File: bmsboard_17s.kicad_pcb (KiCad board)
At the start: 2 copper layers, 100 x 90 mm, 181 parts, among them Q1 Q_NMOS_GDS, Q10 Q_NMOS_GDS, Q11 Q_NMOS_GDS, Q12 Q_NMOS_GDS, Q13 Q_NMOS_GDS, Q14 Q_NMOS_GDS, Q15 Q_NMOS_GDS, Q16 Q_NMOS_GDS, Q17 Q_NMOS_GDS, Q18 Q_NMOS_GDS, Q19 Q_NMOS_GDS, Q2 Q_NMOS_GDS, Q20 Q_NMOS_GDS, Q21 Q_NMOS_GDS, Q22 Q_NMOS_GDS, Q23 Q_NMOS_GDS, Q24 Q_NMOS_GDS, Q25 Q_NMOS_GDS, Q26 Q_NMOS_GDS, Q29 Q_NMOS_GDS, Q3 Q_PMOS_GDS, Q30 Q_NMOS_GDS, Q31 Q_NMOS_GDS, Q32 Q_NMOS_GDS, Q33 Q_NMOS_GDS, Q34 Q_NMOS_GDS, Q35 Q_NMOS_GDS, Q36 Q_NMOS_GDS, Q37 Q_NMOS_GDS, Q38 Q_NMOS_GDS, Q4 Q_NPN_BCE, U1 PB7170, U10 TJA1042T-3, U2 CH32V103C8T6, U3 XTSD01G, U5 BMP280, U7 Si7020-A20, U8 QMA6100P, U9 ADS1243, Y1 16MHz, Y2 32.768kHz

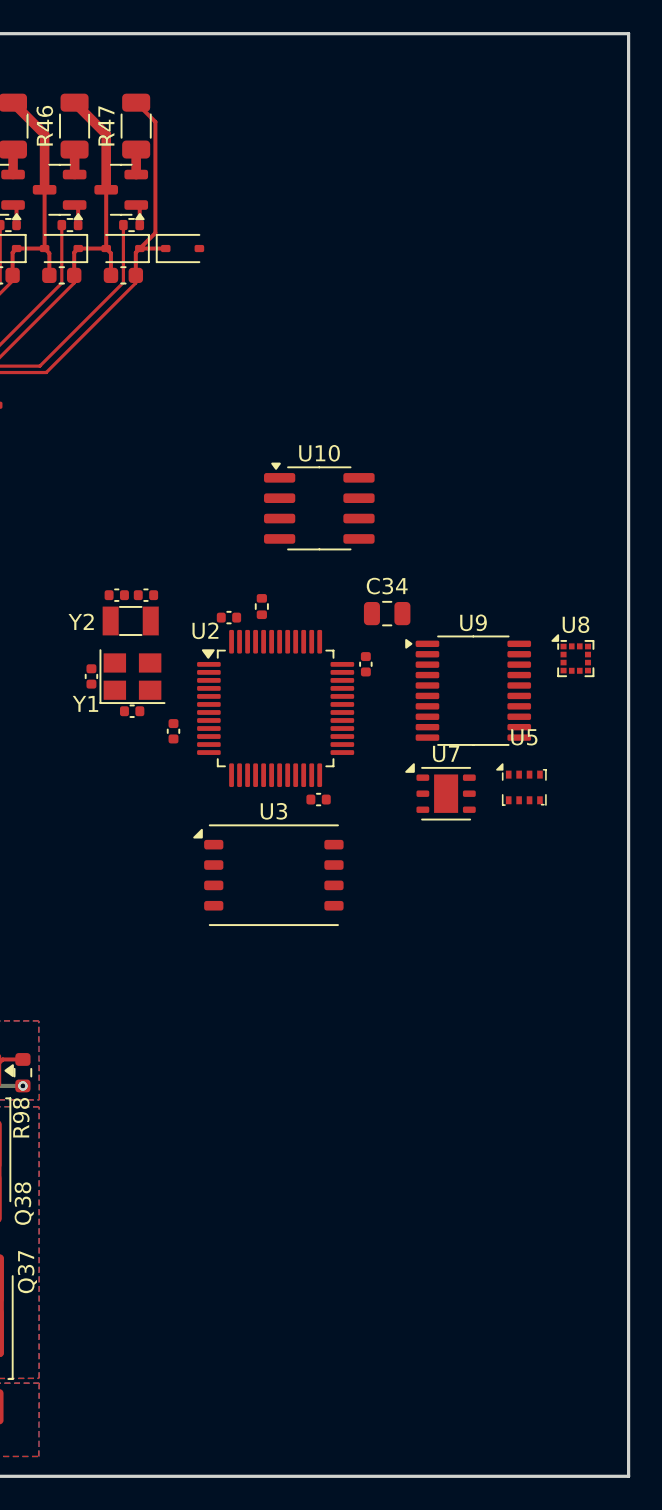
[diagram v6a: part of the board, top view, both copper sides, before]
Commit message: 分配封装和在PCB上大致布局
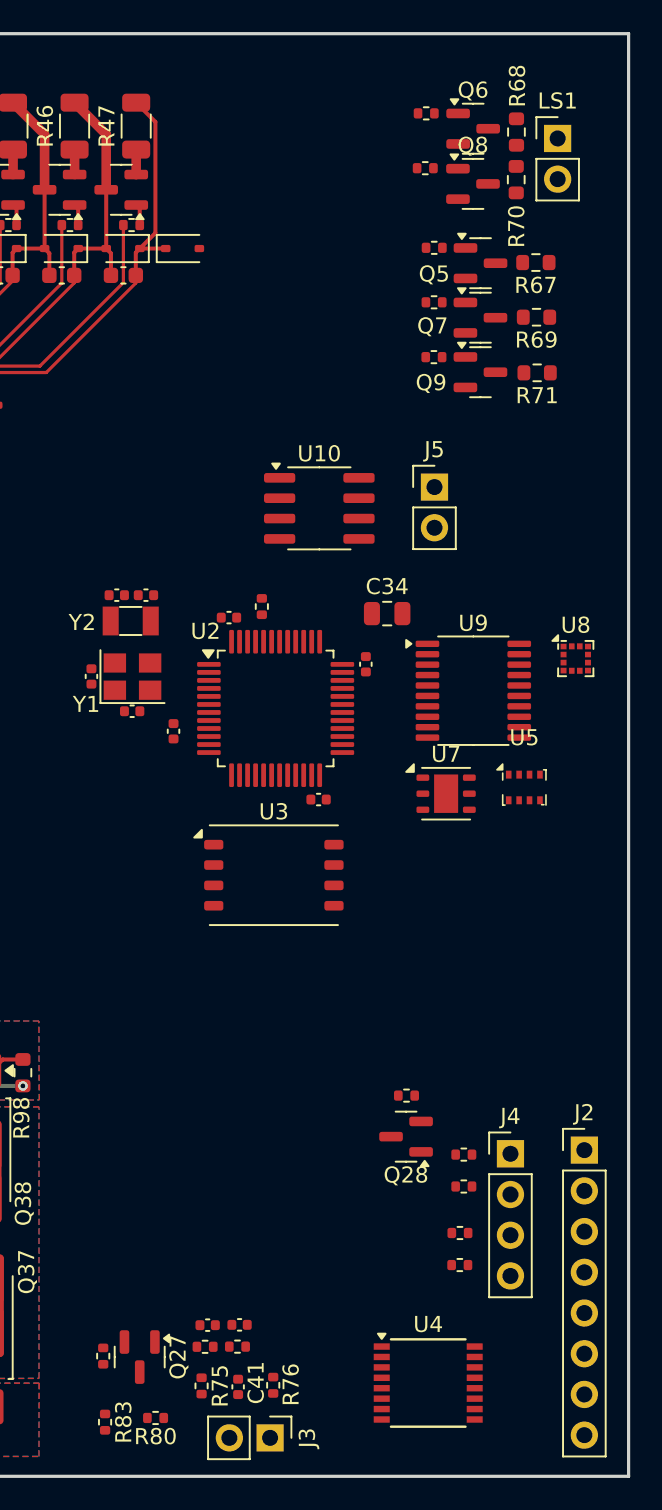
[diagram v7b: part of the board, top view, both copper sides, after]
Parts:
- added C36: 1uF, Capacitor_SMD:C_0402_1005Metric, F.Cu at (96.4, 108.8)
- added C40: 1uF, Capacitor_SMD:C_0402_1005Metric, F.Cu at (98.4, 108.8)
- added C41: 10nF, Capacitor_SMD:C_0402_1005Metric, F.Cu at (98.3, 112.7)
- added J2: Conn_01x08, Connector_PinHeader_2.54mm:PinHeader_1x08_P2.54mm_Vertical, F.Cu at (119.9, 97.9)
- added J3: Conn_01x02, Connector_PinHeader_2.54mm:PinHeader_1x02_P2.54mm_Vertical, F.Cu at (100.3, 115.9)
- added J4: Conn_01x04, Connector_PinHeader_2.54mm:PinHeader_1x04_P2.54mm_Vertical, F.Cu at (115.3, 98.1)
- added J5: Conn_01x02, Connector_PinHeader_2.54mm:PinHeader_1x02_P2.54mm_Vertical, F.Cu at (110.6, 56.5)
- added LS1: Speaker_Crystal, Connector_PinHeader_2.54mm:PinHeader_1x02_P2.54mm_Vertical, F.Cu at (118.3, 34.8)
- added Q27: PMOS, Package_TO_SOT_SMD:SOT-23, F.Cu at (92.2, 110.8)
- added Q28: PMOS, Package_TO_SOT_SMD:SOT-23, F.Cu at (108.8, 97.1)
- added Q5: Q_NPN_BEC, Package_TO_SOT_SMD:SOT-23, F.Cu at (113.5, 42.6)
- added Q6: Q_NPN_BEC, Package_TO_SOT_SMD:SOT-23, F.Cu at (113.0, 34.2)
- added Q7: Q_NPN_BEC, Package_TO_SOT_SMD:SOT-23, F.Cu at (113.4, 46.0)
- added Q8: Q_NPN_BEC, Package_TO_SOT_SMD:SOT-23, F.Cu at (113.0, 37.6)
- added Q9: Q_NPN_BEC, Package_TO_SOT_SMD:SOT-23, F.Cu at (113.4, 49.4)
- added R62: 4.7k, Resistor_SMD:R_0402_1005Metric, F.Cu at (110.5, 48.4)
- added R63: 4.7k, Resistor_SMD:R_0402_1005Metric, F.Cu at (110.6, 45.0)
- added R64: 4.7k, Resistor_SMD:R_0402_1005Metric, F.Cu at (110.6, 41.6)
- added R65: 10k, Resistor_SMD:R_0402_1005Metric, F.Cu at (110.0, 36.7)
- added R66: 10k, Resistor_SMD:R_0402_1005Metric, F.Cu at (110.1, 33.2)
- added R67: 150, Resistor_SMD:R_0603_1608Metric, F.Cu at (116.9, 42.5)
- added R68: 1k, Resistor_SMD:R_0603_1608Metric, F.Cu at (115.7, 34.4)
- added R69: 150, Resistor_SMD:R_0603_1608Metric, F.Cu at (116.9, 46.0)
- added R70: 1k, Resistor_SMD:R_0603_1608Metric, F.Cu at (115.7, 37.4)
- added R71: 150, Resistor_SMD:R_0603_1608Metric, F.Cu at (117.0, 49.4)
- added R72: 100k, Resistor_SMD:R_0402_1005Metric, F.Cu at (89.9, 110.8)
- added R73: 4.7k, Resistor_SMD:R_0402_1005Metric, F.Cu at (96.3, 110.2)
- added R74: 4.7k, Resistor_SMD:R_0402_1005Metric, F.Cu at (98.3, 110.2)
- added R75: 1k, Resistor_SMD:R_0402_1005Metric, F.Cu at (96.0, 112.6)
- added R76: 1k, Resistor_SMD:R_0402_1005Metric, F.Cu at (100.5, 112.6)
- added R77: R, Resistor_SMD:R_0402_1005Metric, F.Cu at (108.8, 94.5)
- added R78: R, Resistor_SMD:R_0402_1005Metric, F.Cu at (112.2, 105.1)
- added R79: R, Resistor_SMD:R_0402_1005Metric, F.Cu at (112.2, 103.1)
- added R80: 1k, Resistor_SMD:R_0402_1005Metric, F.Cu at (93.2, 114.6)
- added R81: R, Resistor_SMD:R_0402_1005Metric, F.Cu at (112.4, 100.2)
- added R82: R, Resistor_SMD:R_0402_1005Metric, F.Cu at (112.4, 98.2)
- added R83: 1k, Resistor_SMD:R_0402_1005Metric, F.Cu at (90.0, 114.9)
- added U4: 74HC138, Package_SO:SSOP-16_4.4x5.2mm_P0.65mm, F.Cu at (110.2, 112.4)
- Q4: value Q_NPN_BCE -> Q_NPN_BEC
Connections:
- Q4 pad 2: Net-(Q4-C) -> +3.3V
- Q4 pad 3: +3.3V -> Net-(Q4-E)
- R50 pad 2: Net-(Q4-C) -> Net-(Q4-E)
- U10 pad 6: unconnected-(U10-CANL-Pad6) -> Net-(J5-Pin_2)
- U10 pad 7: unconnected-(U10-CANH-Pad7) -> Net-(J5-Pin_1)

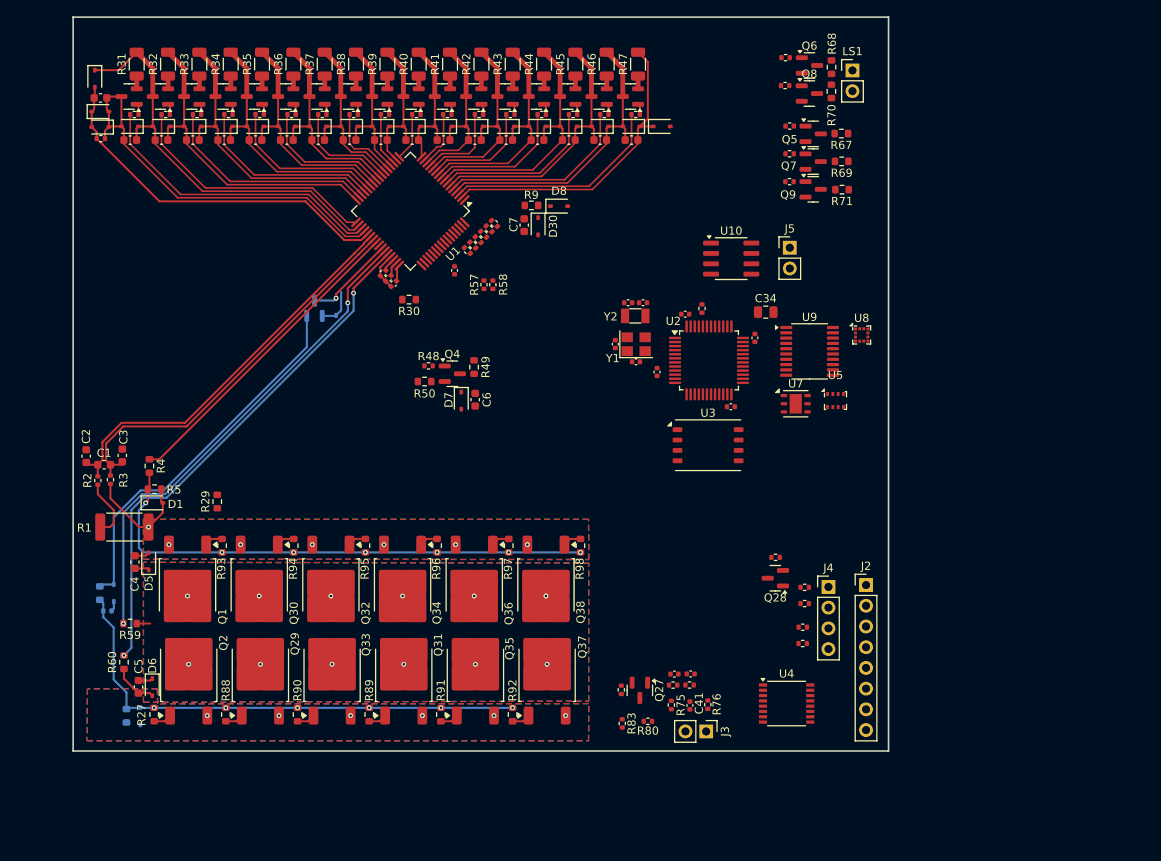
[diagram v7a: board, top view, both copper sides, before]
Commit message: 分配封装，添加RS485通信接口，调整布局，传感器连接到独立MCU上
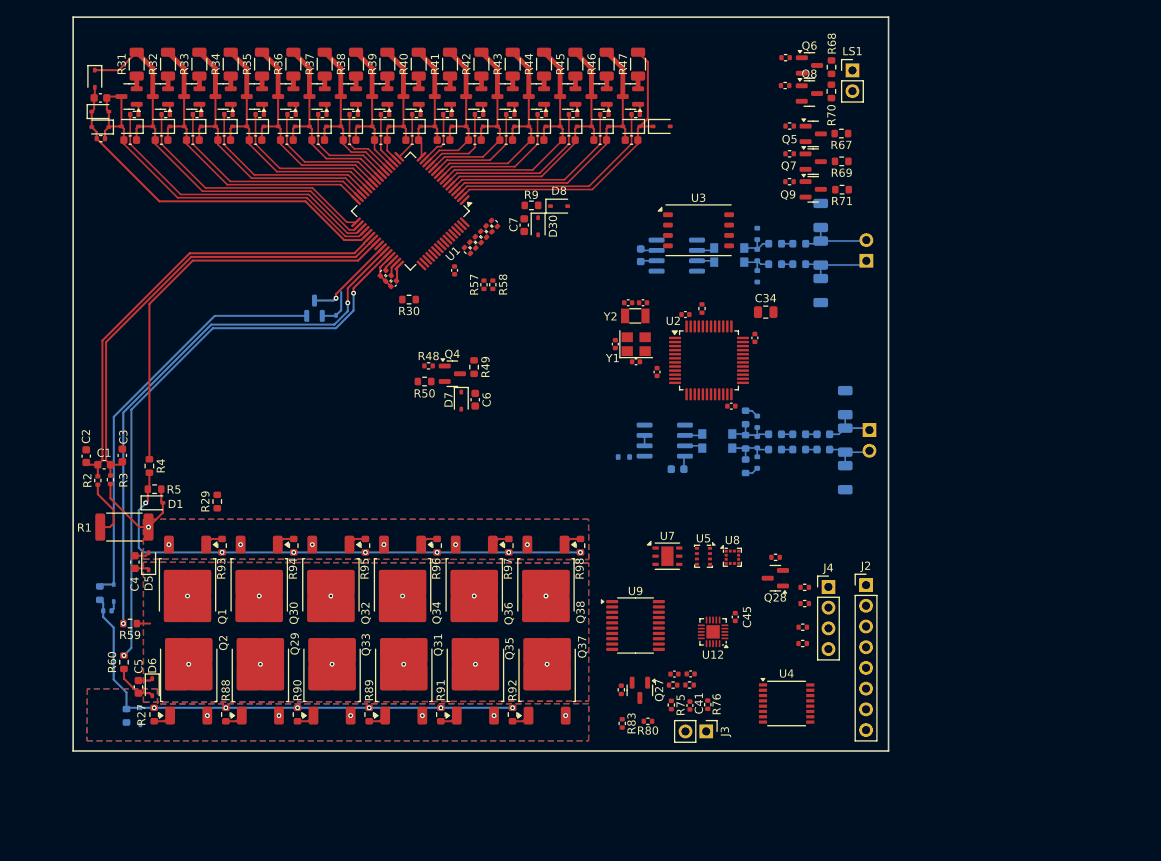
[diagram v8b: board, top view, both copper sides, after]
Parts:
- added C42: C, Capacitor_SMD:C_0603_1608Metric, B.Cu at (96.8, 83.7)
- added C43: 100nF, Capacitor_SMD:C_0603_1608Metric, B.Cu at (114.7, 79.4)
- added C44: 100nF, Capacitor_SMD:C_0603_1608Metric, B.Cu at (114.7, 81.3)
- added C45: 0.1uF, Capacitor_SMD:C_0402_1005Metric, F.Cu at (103.9, 101.8)
- added C46: C, Capacitor_SMD:C_0603_1608Metric, B.Cu at (92.3, 57.5)
- added D32: 2.0V, Diode_SMD:D_SOD-523, B.Cu at (90.2, 82.2)
- added D33: ESD5Zxx, Diode_SMD:D_SOD-523, B.Cu at (106.6, 77.9)
- added D34: ESD5Zxx, Diode_SMD:D_SOD-523, B.Cu at (106.6, 80.4)
- added D35: ESD5Zxx, Diode_SMD:D_SOD-523, B.Cu at (106.6, 82.9)
- added D36: ESD5Zxx, Diode_SMD:D_SOD-523, B.Cu at (106.6, 54.8)
- added D37: ESD5Zxx, Diode_SMD:D_SOD-523, B.Cu at (106.6, 57.4)
- added D38: ESD5Zxx, Diode_SMD:D_SOD-523, B.Cu at (106.6, 60.0)
- added F1: Polyfuse, Fuse:Fuse_0603_1608Metric, B.Cu at (108.8, 79.4)
- added F2: Polyfuse, Fuse:Fuse_0603_1608Metric, B.Cu at (108.8, 81.3)
- added F3: Polyfuse, Fuse:Fuse_0603_1608Metric, B.Cu at (108.8, 58.6)
- added F4: Polyfuse, Fuse:Fuse_0603_1608Metric, B.Cu at (108.8, 56.0)
- added FB1: 120, Inductor_SMD:L_0603_1608Metric, B.Cu at (111.7, 79.4)
- added FB2: 120, Inductor_SMD:L_0603_1608Metric, B.Cu at (111.7, 81.3)
- added FB3: 120, Inductor_SMD:L_0603_1608Metric, B.Cu at (111.7, 58.6)
- added FB4: 120, Inductor_SMD:L_0603_1608Metric, B.Cu at (111.7, 56.0)
- added GD1: GDT_2Pin, Capacitor_SMD:C_1206_3216Metric, B.Cu at (117.4, 75.5)
- added GD2: GDT_2Pin, Capacitor_SMD:C_1206_3216Metric, B.Cu at (117.4, 80.1)
- added GD3: GDT_2Pin, Capacitor_SMD:C_1206_3216Metric, B.Cu at (117.4, 84.7)
- added GD4: GDT_2Pin, Capacitor_SMD:C_1206_3216Metric, B.Cu at (114.4, 61.8)
- added GD5: GDT_2Pin, Capacitor_SMD:C_1206_3216Metric, B.Cu at (114.4, 57.2)
- added GD6: GDT_2Pin, Capacitor_SMD:C_1206_3216Metric, B.Cu at (114.4, 52.6)
- added J6: Conn_01x02, Connector_PinHeader_2.54mm:PinHeader_1x02_P2.54mm_Vertical, B.Cu at (120.3, 78.9)
- added L1: L_Coupled, Inductor_SMD:L_CommonModeChoke_Coilcraft_1812CAN, B.Cu at (101.7, 80.3)
- added L2: L_Coupled, Inductor_SMD:L_CommonModeChoke_Coilcraft_1812CAN, B.Cu at (103.2, 57.5)
- added R101: 1M, Resistor_SMD:R_0603_1608Metric, B.Cu at (105.2, 77.4)
- added R102: 1M, Resistor_SMD:R_0603_1608Metric, B.Cu at (105.2, 80.3)
- added R103: 1M, Resistor_SMD:R_0603_1608Metric, B.Cu at (105.2, 83.3)
- added U11: MAX485E, Package_SO:SOIC-8_3.9x4.9mm_P1.27mm, B.Cu at (95.2, 80.2)
- added U12: PY32F003F1xUx, Package_DFN_QFN:QFN-20-1EP_3x3mm_P0.4mm_EP1.65x1.65mm, F.Cu at (101.2, 103.7)
- J5, U10: moved to B.Cu
- moved U9 39.8 mm to (91.7, 102.9)
- moved U8 31.5 mm to (103.5, 94.5)
- moved U3 26.4 mm to (99.4, 54.4)
- moved U5 25.0 mm to (100.0, 94.4), turned to -90 degrees
- moved U7 24.4 mm to (95.6, 94.4)
- moved J5 9.53 mm to (120.0, 58.1)
- moved U10 6.68 mm to (96.7, 57.5)
- moved C37 0.09 mm to (103.4, 76.0)
- moved C38 0.05 mm to (97.8, 64.7)
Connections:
- J4 pad 1: /RTEMP_OUT3 -> /Sensors Module/RTEMP_OUT3
- J4 pad 2: /RTEMP_OUT2 -> /Sensors Module/RTEMP_OUT2
- J4 pad 3: /RTEMP_OUT1 -> /Sensors Module/RTEMP_OUT1
- J4 pad 4: /RTEMP_OUT0 -> /Sensors Module/RTEMP_OUT0
- Q27 pad 2: /WDET_EN -> /Sensors Module/WDET_EN
- Q28 pad 2: /RTEMP_EN -> /Sensors Module/RTEMP_EN
- R52 pad 1: /AFE Module/MISO -> /MISO
- R54 pad 1: /AFE Module/MOSI -> /MOSI
- R55 pad 1: /AFE Module/CS_AFE -> /CS_AFE
- R56 pad 1: /AFE Module/SCLK -> /SCLK
- R72 pad 1: /WDET_EN -> /Sensors Module/WDET_EN
- R75 pad 1: /WDET_PWM -> /Sensors Module/WDET_PWM
- R77 pad 1: /RTEMP_EN -> /Sensors Module/RTEMP_EN
- R78 pad 2: /RTEMP_OUT0 -> /Sensors Module/RTEMP_OUT0
- R79 pad 2: /RTEMP_OUT1 -> /Sensors Module/RTEMP_OUT1
- R81 pad 2: /RTEMP_OUT2 -> /Sensors Module/RTEMP_OUT2
- R82 pad 2: /RTEMP_OUT3 -> /Sensors Module/RTEMP_OUT3
- R83 pad 2: /WDET_OUT -> /Sensors Module/WDET_OUT
- U10 pad 6: Net-(J5-Pin_2) -> Net-(U10-CANL)
- U10 pad 7: Net-(J5-Pin_1) -> Net-(U10-CANH)
- U2 pad 11: /RTEMP_OUT0 -> unconnected-(U2-PA1-Pad11)
- U2 pad 12: /RTEMP_OUT1 -> unconnected-(U2-PA2-Pad12)
- U2 pad 13: /RTEMP_OUT2 -> unconnected-(U2-PA3-Pad13)
- U2 pad 14: /RTEMP_OUT3 -> unconnected-(U2-PA4-Pad14)
- U2 pad 15: /WDET_OUT -> unconnected-(U2-PA5-Pad15)
- U2 pad 19: /WDET_PWM -> /MCU Module/WDET_PWM
- U2 pad 20: /WDET_EN -> /MCU Module/WDET_EN
- U2 pad 25: /RTEMP_R0 -> unconnected-(U2-PB12-Pad25)
- U2 pad 26: /RTEMP_R1 -> unconnected-(U2-PB13-Pad26)
- U2 pad 27: /RTEMP_R2 -> unconnected-(U2-PB14-Pad27)
- U2 pad 28: /RTEMP_EN -> /MCU Module/CS_SD
- U3 pad 2: unconnected-(U3-SD3/~{CS}-Pad2) -> /MCU Module/CS_SD
- U3 pad 3: unconnected-(U3-CLK-Pad3) -> /SCLK
- U3 pad 5: unconnected-(U3-CMD/DI-Pad5) -> /MOSI
- U3 pad 6: unconnected-(U3-SD0/DO-Pad6) -> /MISO
- U4 pad 1: /RTEMP_R0 -> /Sensors Module/RTEMP_R0
- U4 pad 2: /RTEMP_R1 -> /Sensors Module/RTEMP_R1
- U4 pad 3: /RTEMP_R2 -> /Sensors Module/RTEMP_R2
- U4 pad 4: /RTEMP_EN -> /Sensors Module/RTEMP_EN
- U5 pad 3: /SDA1 -> /Sensors Module/SDA
- U5 pad 4: /SCL1 -> /Sensors Module/SCL
- U7 pad 1: /SDA1 -> /Sensors Module/SDA
- U7 pad 6: /SCL1 -> /Sensors Module/SCL
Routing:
- net /AFE Module/DSG: track 38.8 -> 50.0 mm
- net Net-(J5-Pin_1): track 0.00 -> 9.36 mm
- net Net-(J5-Pin_2): track 0.00 -> 9.28 mm
- net /AFE Module/SRN: track 48.9 -> 56.2 mm
- net /AFE Module/SRP: track 49.3 -> 56.6 mm
- net /AFE Module/LODD: track 60.6 -> 67.8 mm
- net /AFE Module/CHGD: track 64.3 -> 71.5 mm
- net Net-(D33-K): track 0.00 -> 7.15 mm
- net Net-(D34-A): track 0.00 -> 7.05 mm
- net Net-(J6-Pin_1): track 0.00 -> 6.95 mm
- net Net-(J6-Pin_2): track 0.00 -> 6.74 mm
- net GND: track 50.3 -> 55.6 mm
- net Net-(D4-A): track 46.2 -> 51.2 mm
- net Net-(D36-K): track 0.00 -> 4.55 mm
- net Net-(D37-K): track 0.00 -> 4.45 mm
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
